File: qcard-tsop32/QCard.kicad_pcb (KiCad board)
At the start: 2 copper layers, 55 x 45 mm, 6 parts, among them J1 Conn_02x18_Top_Bottom, U1 SST39SF040

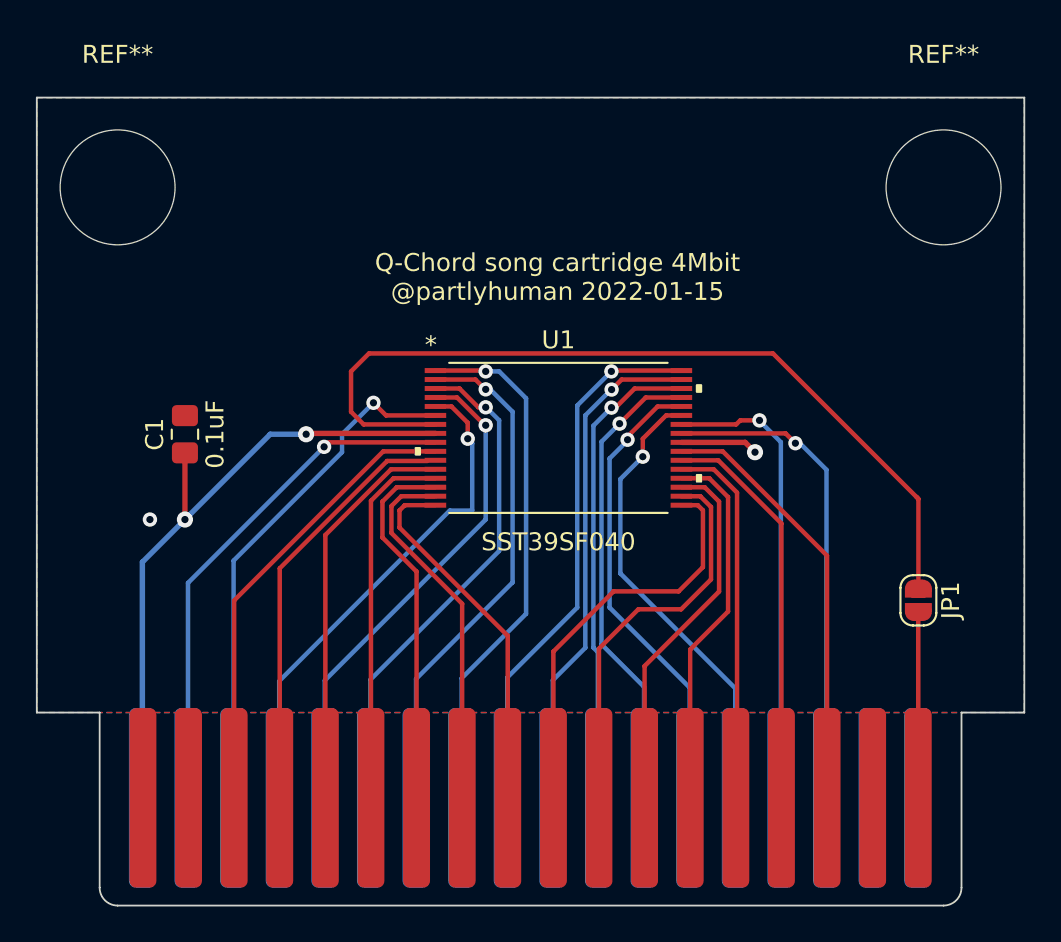
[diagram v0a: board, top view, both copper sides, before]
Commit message: Better write protect jumper behaviour, using text vars
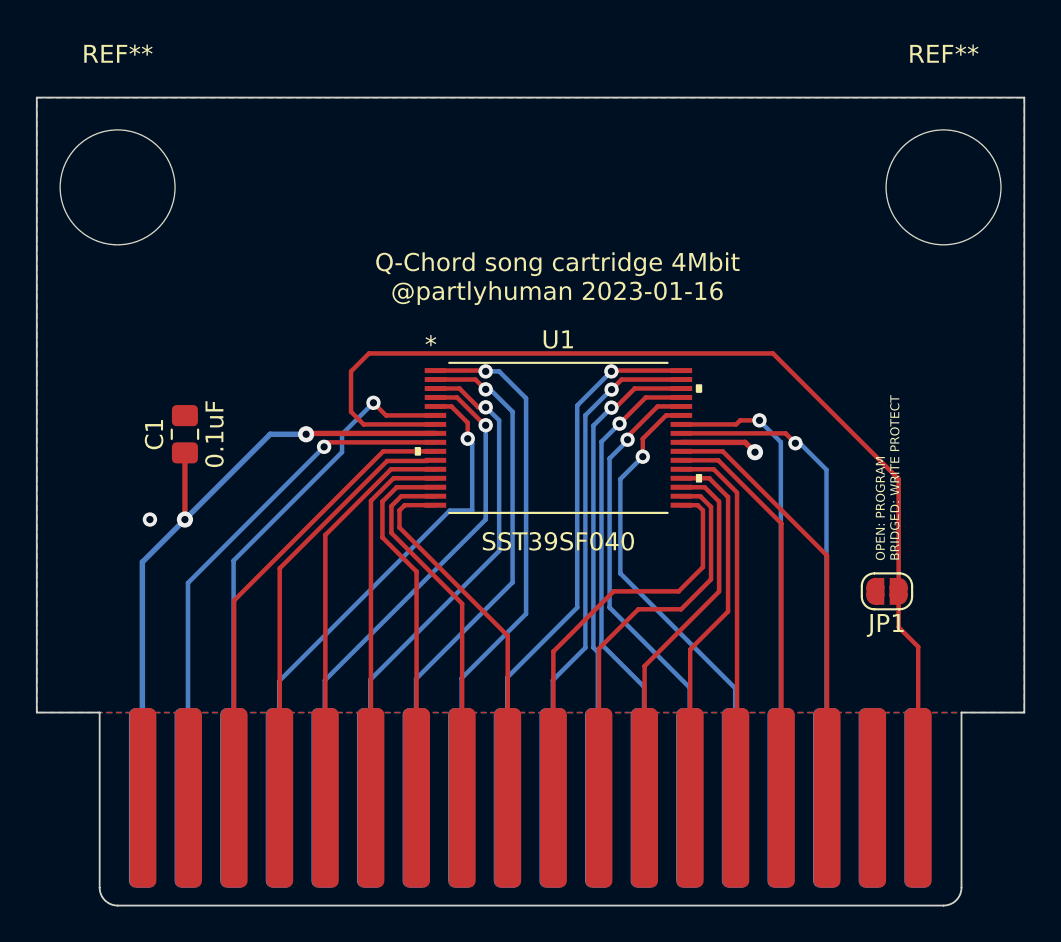
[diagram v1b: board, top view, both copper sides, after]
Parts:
- moved JP1 1.82 mm to (97.3, 77.5), turned to 180 degrees
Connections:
- JP1 pad 1: Net-(U1-Pad7) -> /PGM
- JP1 pad 2: /PGM -> /GND
- U1 pad 7: Net-(U1-Pad7) -> /PGM
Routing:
- net /PGM: track 10.4 -> 59.3 mm
- net Net-(U1-Pad7): track 47.7 -> 0.00 mm
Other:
- board text added: "OPEN: PROGRAM BRIDGED: WRITE PROTECT"
- board text added: "Q-Chord song cartridge 4Mbit ${COMPANY} ${ISSUE_DATE}"
- board text removed: "Q-Chord song cartridge 4Mbit @partlyhuman 2022-01-15"
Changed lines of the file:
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@@
   )
   (paper "USLetter")
+  (title_block
+    (title "Q-Card 4Mbit Flash")
+    (date "2023-01-16")
+    (company "@partlyhuman")
+  )
   (layers
     (0 "F.Cu" signal)
@@
   (net 31 "/D4")
   (net 32 "/D3")
-  (net 33 "Net-(U1-Pad7)")
   (footprint "Jumper:SolderJumper-2_P1.3mm_Open_RoundedPad1.0x1.5mm" (layer "F.Cu")
-    (at 99.1 78 -90)
+    (at 97.35 77.5 180)
     (descr "SMD Solder Jumper, 1x1.5mm, rounded Pads, 0.3mm gap, open")
     (tags "solder jumper open")
@@
     (property "Sheetname" "")
     (attr exclude_from_pos_files)
-    (fp_text reference "JP1" (at 0 -1.8 90) (layer "F.SilkS")
-      (effects (font (size 1 1) (thickness 0.15)))
-    )
-    (fp_text value "SolderJumper_2_Open" (at 0 1.9 90) (layer "F.Fab")
+    (fp_text reference "JP1" (at 0 -1.8) (layer "F.SilkS")
+      (effects (font (size 1 1) (thickness 0.15)))
+    )
+    (fp_text value "SolderJumper_2_Open" (at 0 1.9) (layer "F.Fab")
       (effects (font (size 1 1) (thickness 0.15)))
     )
@@
     (fp_line (start -1.65 -1.25) (end 1.65 -1.25) (layer "F.CrtYd") (width 0.05))
     (fp_line (start 1.65 1.25) (end 1.65 -1.25) (layer "F.CrtYd") (width 0.05))
-    (pad "1" smd custom (at -0.65 0 270) (size 1 0.5) (layers "F.Cu" "F.Mask")
-      (net 33 "Net-(U1-Pad7)") (pinfunction "A") (pintype "passive") (zone_connect 2)
+    (pad "1" smd custom (at -0.65 0 180) (size 1 0.5) (layers "F.Cu" "F.Mask")
+      (net 17 "/PGM") (pinfunction "A") (pintype "passive") (zone_connect 2)
       (options (clearance outline) (anchor rect))
       (primitives
@@
           ) (width 0) (fill yes))
       ))
-    (pad "2" smd custom (at 0.65 0 270) (size 1 0.5) (layers "F.Cu" "F.Mask")
-      (net 17 "/PGM") (pinfunction "B") (pintype "passive") (zone_connect 2)
+    (pad "2" smd custom (at 0.65 0 180) (size 1 0.5) (layers "F.Cu" "F.Mask")
+      (net 2 "/GND") (pinfunction "B") (pintype "passive") (zone_connect 2)
       (options (clearance outline) (anchor rect))
       (primitives
@@
       (net 19 "/A17") (pinfunction "A17") (pintype "input"))
     (pad "7" smd rect locked (at -6.848848 -0.750001) (size 1.200899 0.2794) (layers "F.Cu" "F.Paste" "F.Mask")
-      (net 33 "Net-(U1-Pad7)") (pinfunction "*WE") (pintype "unspecified"))
+      (net 17 "/PGM") (pinfunction "*WE") (pintype "unspecified"))
     (pad "8" smd rect locked (at -6.848848 -0.25) (size 1.200899 0.2794) (layers "F.Cu" "F.Paste" "F.Mask")
       (net 1 "/VCC") (pinfunction "VDD") (pintype "power_in"))
@@
   (gr_line (start 53.5 84.25) (end 53.5 94) (layer "Edge.Cuts") (width 0.1))
   (gr_line (start 101.5 94) (end 101.5 84.25) (layer "Edge.Cuts") (width 0.1))
-  (gr_text "Q-Chord song cartridge 4Mbit\n@partlyhuman 2022-01-15" (at 79 60) (layer "F.SilkS")
+  (gr_text "Q-Chord song cartridge 4Mbit\n${COMPANY} ${ISSUE_DATE}" (at 79 60) (layer "F.SilkS")
     (effects (font (size 1 1) (thickness 0.15)))
+  )
+  (gr_text "OPEN: PROGRAM\nBRIDGED: WRITE PROTECT" (at 97.4 75.8 90) (layer "F.SilkS")
+    (effects (font (size 0.5 0.5) (thickness 0.125)) (justify left))
   )
   (segment (start 65 68.75) (end 65.0475 68.7025) (width 0.3) (layer "F.Cu") (net 1))
@@
   (segment (start 94.01 89) (end 94.01 75.51) (width 0.25) (layer "F.Cu") (net 16))
   (segment (start 94.01 75.51) (end 88.202501 69.702501) (width 0.25) (layer "F.Cu") (net 16))
-  (segment (start 99.09 89) (end 99.09 78.66) (width 0.25) (layer "F.Cu") (net 17))
-  (segment (start 99.09 78.66) (end 99.1 78.65) (width 0.25) (layer "F.Cu") (net 17))
+  (segment (start 98 77.5) (end 98 71.25) (width 0.25) (layer "F.Cu") (net 17))
+  (segment (start 68.5 64.25) (end 67.5 65.25) (width 0.25) (layer "F.Cu") (net 17))
+  (segment (start 91 64.25) (end 68.5 64.25) (width 0.25) (layer "F.Cu") (net 17))
+  (segment (start 99.09 80.59) (end 98 79.5) (width 0.25) (layer "F.Cu") (net 17))
+  (segment (start 67.5 65.25) (end 67.5 67.5) (width 0.25) (layer "F.Cu") (net 17))
+  (segment (start 99.09 89) (end 99.09 80.59) (width 0.25) (layer "F.Cu") (net 17))
+  (segment (start 68.202499 68.202499) (end 72.201377 68.202499) (width 0.25) (layer "F.Cu") (net 17))
+  (segment (start 98 71.25) (end 91 64.25) (width 0.25) (layer "F.Cu") (net 17))
+  (segment (start 67.5 67.5) (end 68.202499 68.202499) (width 0.25) (layer "F.Cu") (net 17))
+  (segment (start 98 79.5) (end 98 77.5) (width 0.25) (layer "F.Cu") (net 17))
   (segment (start 66.2495 69.2025) (end 72.201377 69.2025) (width 0.25) (layer "F.Cu") (net 18))
   (segment (start 66 69.452) (end 66.2495 69.2025) (width 0.25) (layer "F.Cu") (net 18))
@@
   (segment (start 92.5 69.25) (end 93.98 70.73) (width 0.25) (layer "B.Cu") (net 32))
   (segment (start 93.98 70.73) (end 93.98 89) (width 0.25) (layer "B.Cu") (net 32))
-  (segment (start 68.202499 68.202499) (end 67.5 67.5) (width 0.25) (layer "F.Cu") (net 33))
-  (segment (start 68.5 64.25) (end 91 64.25) (width 0.25) (layer "F.Cu") (net 33))
-  (segment (start 99 72.25) (end 99.09 72.34) (width 0.25) (layer "F.Cu") (net 33))
-  (segment (start 91 64.25) (end 99 72.25) (width 0.25) (layer "F.Cu") (net 33))
-  (segment (start 67.5 65.25) (end 68.5 64.25) (width 0.25) (layer "F.Cu") (net 33))
-  (segment (start 99.1 77.35) (end 99.1 72.35) (width 0.25) (layer "F.Cu") (net 33))
-  (segment (start 72.201377 68.202499) (end 68.202499 68.202499) (width 0.25) (layer "F.Cu") (net 33))
-  (segment (start 99.1 72.35) (end 99 72.25) (width 0.25) (layer "F.Cu") (net 33))
-  (segment (start 67.5 67.5) (end 67.5 65.25) (width 0.25) (layer "F.Cu") (net 33))
   (zone (net 2) (net_name "/GND") (layers F&B.Cu) (hatch edge 0.508)
     (connect_pads (clearance 0.508))

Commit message: Pulling WE high for reading per datasheet
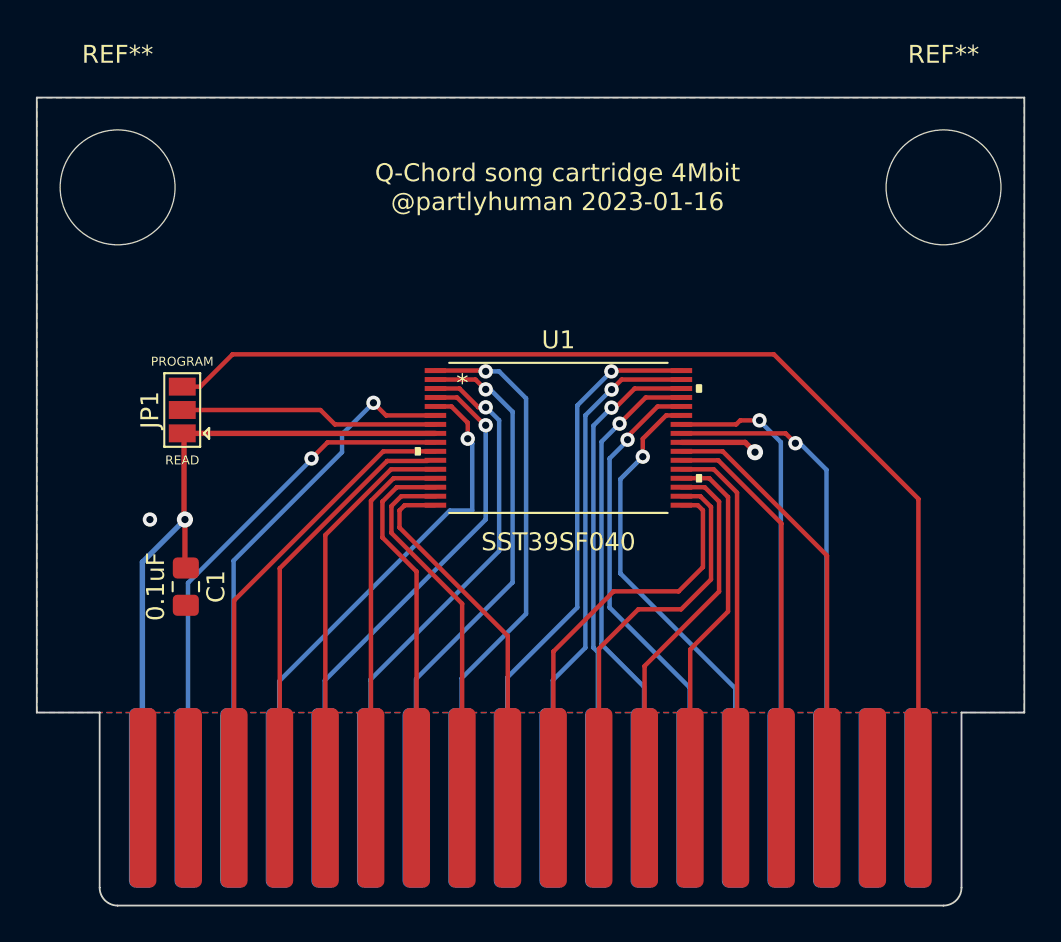
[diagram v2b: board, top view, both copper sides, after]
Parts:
- JP1: value SolderJumper_2_Open -> SolderJumper_3_Open; footprint Jumper:SolderJumper-2_P1.3mm_Open_RoundedPad1.0x1.5mm -> Jumper:SolderJumper-3_P1.3mm_Open_Pad1.0x1.5mm
- moved JP1 40.5 mm to (58.1, 67.4), turned to 90 degrees
- moved C1 8.49 mm to (58.3, 77.2), turned to -90 degrees
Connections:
- J1 pad 18: /PGM -> Net-(J1-Pad18)
- JP1 pad 1: /PGM -> /VCC
- JP1 pad 2: /GND -> /PGM
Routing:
- net Net-(J1-Pad18): track 0.00 -> 61.7 mm
- net /PGM: track 59.3 -> 14.4 mm
- net /VCC: track 36.1 -> 38.2 mm, vias 2 -> 1
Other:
- board text added: "PROGRAM"
- board text added: "READ"
- board text removed: "OPEN: PROGRAM BRIDGED: WRITE PROTECT"
